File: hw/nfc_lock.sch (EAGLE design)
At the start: 37 parts, among them IC1 STM8S003F3, IC3 MCP170312MB, Q1 8MHz, Q3 2N7002,215, U1 M24SR16-YMN6T/2, U2 2N7002,215, U3 2N7002,215, U4 IRFML8244TRPBF, X1 MINI-USB-32005-301

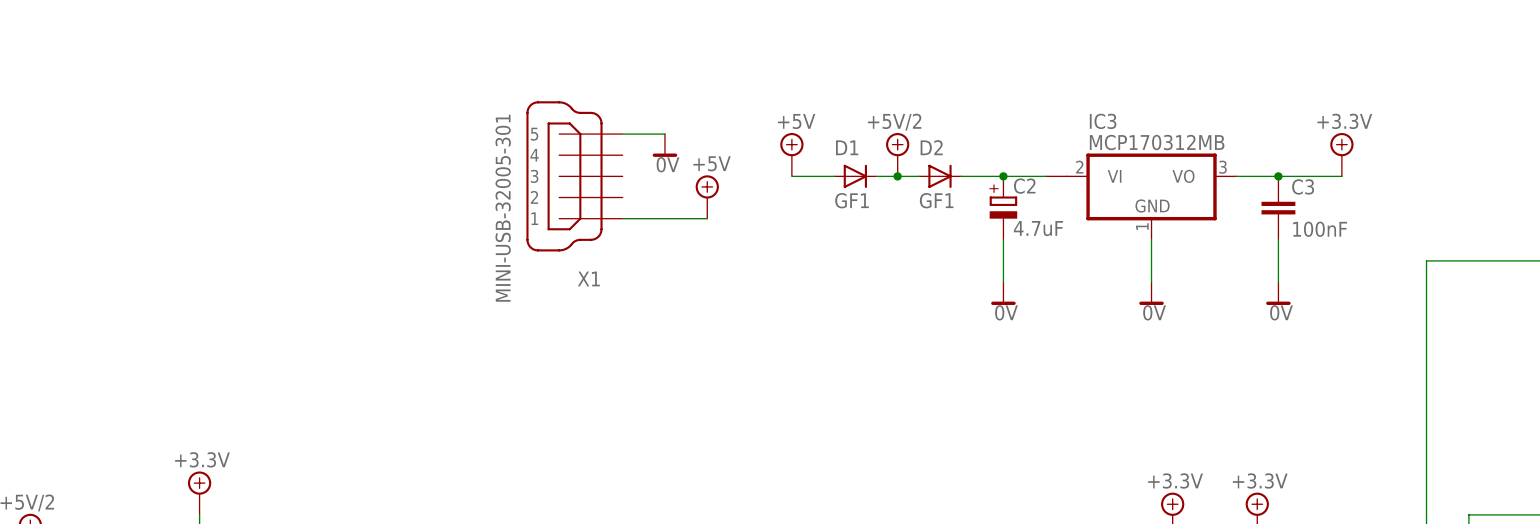
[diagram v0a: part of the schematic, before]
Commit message: additional 4.7uF for general power decoupling
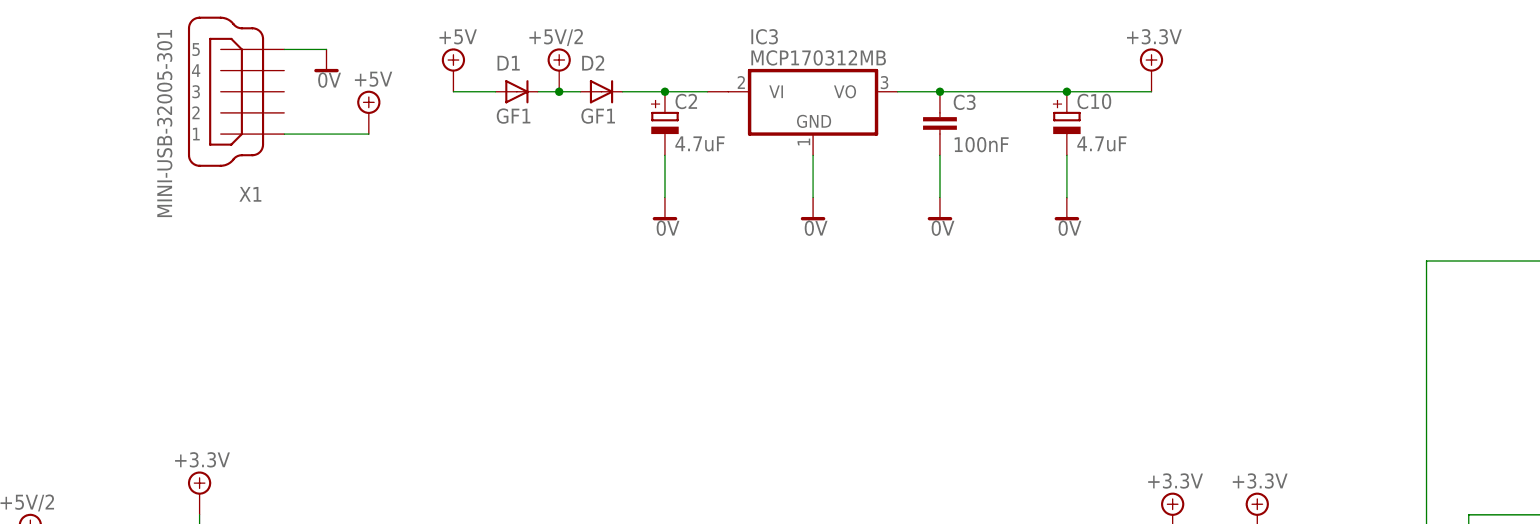
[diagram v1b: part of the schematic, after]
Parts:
- added C10: 4.7uF, rcl:CPOL-EU153CLV-0405
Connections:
- net +5V/1: now also C10.+
- net 0V: now also C10.-
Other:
- moved on the sheet: C2, C3, D1, D2, IC3, X1
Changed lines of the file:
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@@
 <part name="SUPPLY37" library="supply2" deviceset="0V" device=""/>
 <part name="SUPPLY40" library="supply2" deviceset="0V" device=""/>
+<part name="C10" library="rcl" deviceset="CPOL-EU" device="153CLV-0405" value="4.7uF"/>
+<part name="SUPPLY41" library="supply2" deviceset="0V" device=""/>
 </parts>
 <sheets>
@@
 <instance part="U1" gate="G$1" x="134.62" y="78.74"/>
 <instance part="IC1" gate="G$1" x="22.86" y="76.2"/>
-<instance part="IC3" gate="G$1" x="71.12" y="154.94"/>
-<instance part="SUPPLY1" gate="+5V" x="27.94" y="157.48"/>
-<instance part="SUPPLY2" gate="G$1" x="93.98" y="157.48"/>
-<instance part="SUPPLY3" gate="0V" x="71.12" y="139.7"/>
-<instance part="C2" gate="G$1" x="53.34" y="152.4"/>
-<instance part="C3" gate="G$1" x="86.36" y="152.4"/>
-<instance part="D1" gate="D" x="35.56" y="154.94"/>
-<instance part="D2" gate="D" x="45.72" y="154.94"/>
-<instance part="SUPPLY4" gate="0V" x="86.36" y="139.7"/>
-<instance part="SUPPLY5" gate="0V" x="53.34" y="139.7"/>
-<instance part="SUPPLY6" gate="0V" x="12.7" y="157.48"/>
-<instance part="SUPPLY7" gate="+5V" x="17.78" y="152.4"/>
-<instance part="X1" gate="G$1" x="2.54" y="154.94" rot="R180"/>
+<instance part="IC3" gate="G$1" x="30.48" y="165.1"/>
+<instance part="SUPPLY1" gate="+5V" x="-12.7" y="167.64"/>
+<instance part="SUPPLY2" gate="G$1" x="71.12" y="167.64"/>
+<instance part="SUPPLY3" gate="0V" x="30.48" y="149.86"/>
+<instance part="C2" gate="G$1" x="12.7" y="162.56"/>
+<instance part="C3" gate="G$1" x="45.72" y="162.56"/>
+<instance part="D1" gate="D" x="-5.08" y="165.1"/>
+<instance part="D2" gate="D" x="5.08" y="165.1"/>
+<instance part="SUPPLY4" gate="0V" x="45.72" y="149.86"/>
+<instance part="SUPPLY5" gate="0V" x="12.7" y="149.86"/>
+<instance part="SUPPLY6" gate="0V" x="-27.94" y="167.64"/>
+<instance part="SUPPLY7" gate="+5V" x="-22.86" y="162.56"/>
+<instance part="X1" gate="G$1" x="-38.1" y="165.1" rot="R180"/>
 <instance part="SUPPLY8" gate="G$1" x="-22.86" y="88.9"/>
 <instance part="SUPPLY9" gate="0V" x="-10.16" y="68.58"/>
@@
 <instance part="U3" gate="G$1" x="-88.9" y="12.7" rot="MR0"/>
 <instance part="SUPPLY14" gate="0V" x="-91.44" y="-10.16"/>
-<instance part="SUPPLY15" gate="G$1" x="40.64" y="157.48"/>
+<instance part="SUPPLY15" gate="G$1" x="0" y="167.64"/>
 <instance part="SUPPLY16" gate="G$1" x="-111.76" y="30.48"/>
 <instance part="R2" gate="G$1" x="-76.2" y="0" rot="R90"/>
@@
 <instance part="SUPPLY37" gate="0V" x="182.88" y="93.98"/>
 <instance part="SUPPLY40" gate="0V" x="193.04" y="93.98"/>
+<instance part="C10" gate="G$1" x="60.96" y="162.56"/>
+<instance part="SUPPLY41" gate="0V" x="60.96" y="149.86"/>
 </instances>
 <busses>
@@
 <pinref part="IC3" gate="G$1" pin="GND"/>
 <pinref part="SUPPLY3" gate="0V" pin="0V"/>
-<wire x1="71.12" y1="142.24" x2="71.12" y2="147.32" width="0.1524" layer="91"/>
+<wire x1="30.48" y1="152.4" x2="30.48" y2="157.48" width="0.1524" layer="91"/>
 </segment>
 <segment>
 <pinref part="C3" gate="G$1" pin="2"/>
 <pinref part="SUPPLY4" gate="0V" pin="0V"/>
-<wire x1="86.36" y1="142.24" x2="86.36" y2="147.32" width="0.1524" layer="91"/>
+<wire x1="45.72" y1="152.4" x2="45.72" y2="157.48" width="0.1524" layer="91"/>
 </segment>
 <segment>
 <pinref part="C2" gate="G$1" pin="-"/>
 <pinref part="SUPPLY5" gate="0V" pin="0V"/>
-<wire x1="53.34" y1="142.24" x2="53.34" y2="147.32" width="0.1524" layer="91"/>
+<wire x1="12.7" y1="152.4" x2="12.7" y2="157.48" width="0.1524" layer="91"/>
 </segment>
 <segment>
 <pinref part="X1" gate="G$1" pin="5"/>
 <pinref part="SUPPLY6" gate="0V" pin="0V"/>
-<wire x1="12.7" y1="160.02" x2="7.62" y2="160.02" width="0.1524" layer="91"/>
+<wire x1="-27.94" y1="170.18" x2="-33.02" y2="170.18" width="0.1524" layer="91"/>
 </segment>
 <segment>
@@
 <wire x1="193.04" y1="96.52" x2="193.04" y2="99.06" width="0.1524" layer="91"/>
 </segment>
+<segment>
+<pinref part="C10" gate="G$1" pin="-"/>
+<pinref part="SUPPLY41" gate="0V" pin="0V"/>
+<wire x1="60.96" y1="152.4" x2="60.96" y2="157.48" width="0.1524" layer="91"/>
+</segment>
 </net>
 <net name="+5V/1" class="0">
@@
 <pinref part="IC3" gate="G$1" pin="VO"/>
 <pinref part="SUPPLY2" gate="G$1" pin="+5V/1"/>
-<wire x1="93.98" y1="154.94" x2="86.36" y2="154.94" width="0.1524" layer="91"/>
+<wire x1="71.12" y1="165.1" x2="60.96" y2="165.1" width="0.1524" layer="91"/>
 <pinref part="C3" gate="G$1" pin="1"/>
-<wire x1="86.36" y1="154.94" x2="81.28" y2="154.94" width="0.1524" layer="91"/>
-<junction x="86.36" y="154.94"/>
+<wire x1="60.96" y1="165.1" x2="45.72" y2="165.1" width="0.1524" layer="91"/>
+<wire x1="45.72" y1="165.1" x2="40.64" y2="165.1" width="0.1524" layer="91"/>
+<junction x="45.72" y="165.1"/>
+<pinref part="C10" gate="G$1" pin="+"/>
+<junction x="60.96" y="165.1"/>
 </segment>
 <segment>
@@
 <pinref part="SUPPLY1" gate="+5V" pin="+5V"/>
 <pinref part="D1" gate="D" pin="A"/>
-<wire x1="33.02" y1="154.94" x2="27.94" y2="154.94" width="0.1524" layer="91"/>
+<wire x1="-7.62" y1="165.1" x2="-12.7" y2="165.1" width="0.1524" layer="91"/>
 </segment>
 <segment>
 <pinref part="X1" gate="G$1" pin="1"/>
 <pinref part="SUPPLY7" gate="+5V" pin="+5V"/>
-<wire x1="17.78" y1="149.86" x2="7.62" y2="149.86" width="0.1524" layer="91"/>
+<wire x1="-22.86" y1="160.02" x2="-33.02" y2="160.02" width="0.1524" layer="91"/>
 </segment>
 </net>
@@
 <pinref part="IC3" gate="G$1" pin="VI1"/>
 <pinref part="D2" gate="D" pin="C"/>
-<wire x1="48.26" y1="154.94" x2="53.34" y2="154.94" width="0.1524" layer="91"/>
+<wire x1="7.62" y1="165.1" x2="12.7" y2="165.1" width="0.1524" layer="91"/>
 <pinref part="C2" gate="G$1" pin="+"/>
-<wire x1="53.34" y1="154.94" x2="58.42" y2="154.94" width="0.1524" layer="91"/>
-<junction x="53.34" y="154.94"/>
+<wire x1="12.7" y1="165.1" x2="17.78" y2="165.1" width="0.1524" layer="91"/>
+<junction x="12.7" y="165.1"/>
 </segment>
 </net>
@@
 <pinref part="D1" gate="D" pin="C"/>
 <pinref part="D2" gate="D" pin="A"/>
-<wire x1="43.18" y1="154.94" x2="40.64" y2="154.94" width="0.1524" layer="91"/>
+<wire x1="2.54" y1="165.1" x2="0" y2="165.1" width="0.1524" layer="91"/>
 <pinref part="SUPPLY15" gate="G$1" pin="+5V/2"/>
-<wire x1="40.64" y1="154.94" x2="38.1" y2="154.94" width="0.1524" layer="91"/>
-<junction x="40.64" y="154.94"/>
-</segment>
-<segment>
+<wire x1="0" y1="165.1" x2="-2.54" y2="165.1" width="0.1524" layer="91"/>
+<junction x="0" y="165.1"/>
+</segment>
+<segment>

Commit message: quartz's capacitors changed from 0402 to 0603K
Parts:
- C5, C8: device rcl:C-EUC0402 -> rcl:C-EUC0603K
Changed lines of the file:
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@@
 <part name="SUPPLY36" library="supply2" deviceset="+5V/2" device=""/>
 <part name="Q3" library="Common-Parts-Library-Eagle" deviceset="2N7002,215" device=""/>
-<part name="C8" library="rcl" deviceset="C-EU" device="C0402" value="33pF"/>
-<part name="C5" library="rcl" deviceset="C-EU" device="C0402" value="33pF"/>
+<part name="C8" library="rcl" deviceset="C-EU" device="C0603K" value="33pF"/>
+<part name="C5" library="rcl" deviceset="C-EU" device="C0603K" value="33pF"/>
 <part name="U4" library="irfml8244trpbf" deviceset="IRFML8244TRPBF" device=""/>
 <part name="R9" library="rcl" deviceset="R-EU_" device="R0805" value="10k"/>
